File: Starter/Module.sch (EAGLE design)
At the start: 3 parts

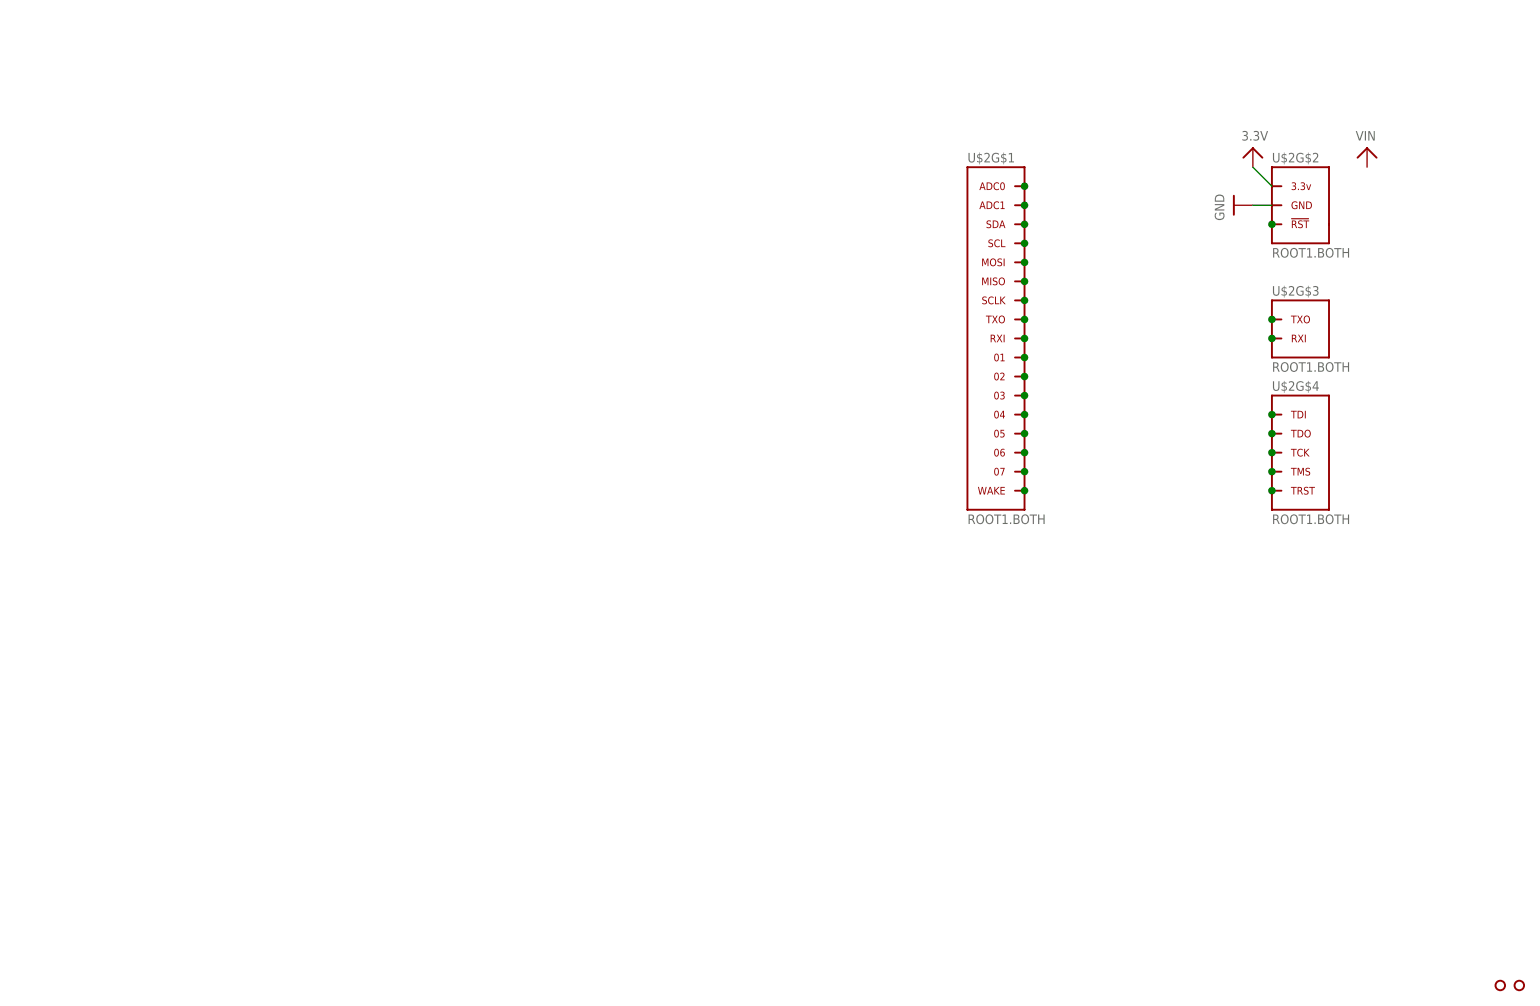
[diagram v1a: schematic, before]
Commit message: Investigating idea to get rid of solder jumpers. Using LoKi Plank scheme of EEPROM and LFSF to auto-assign pins. Also moving to using two connectors instead of one for conector integrety nd module stability. EEPROM: CAT24C02 XOR: NC7S86
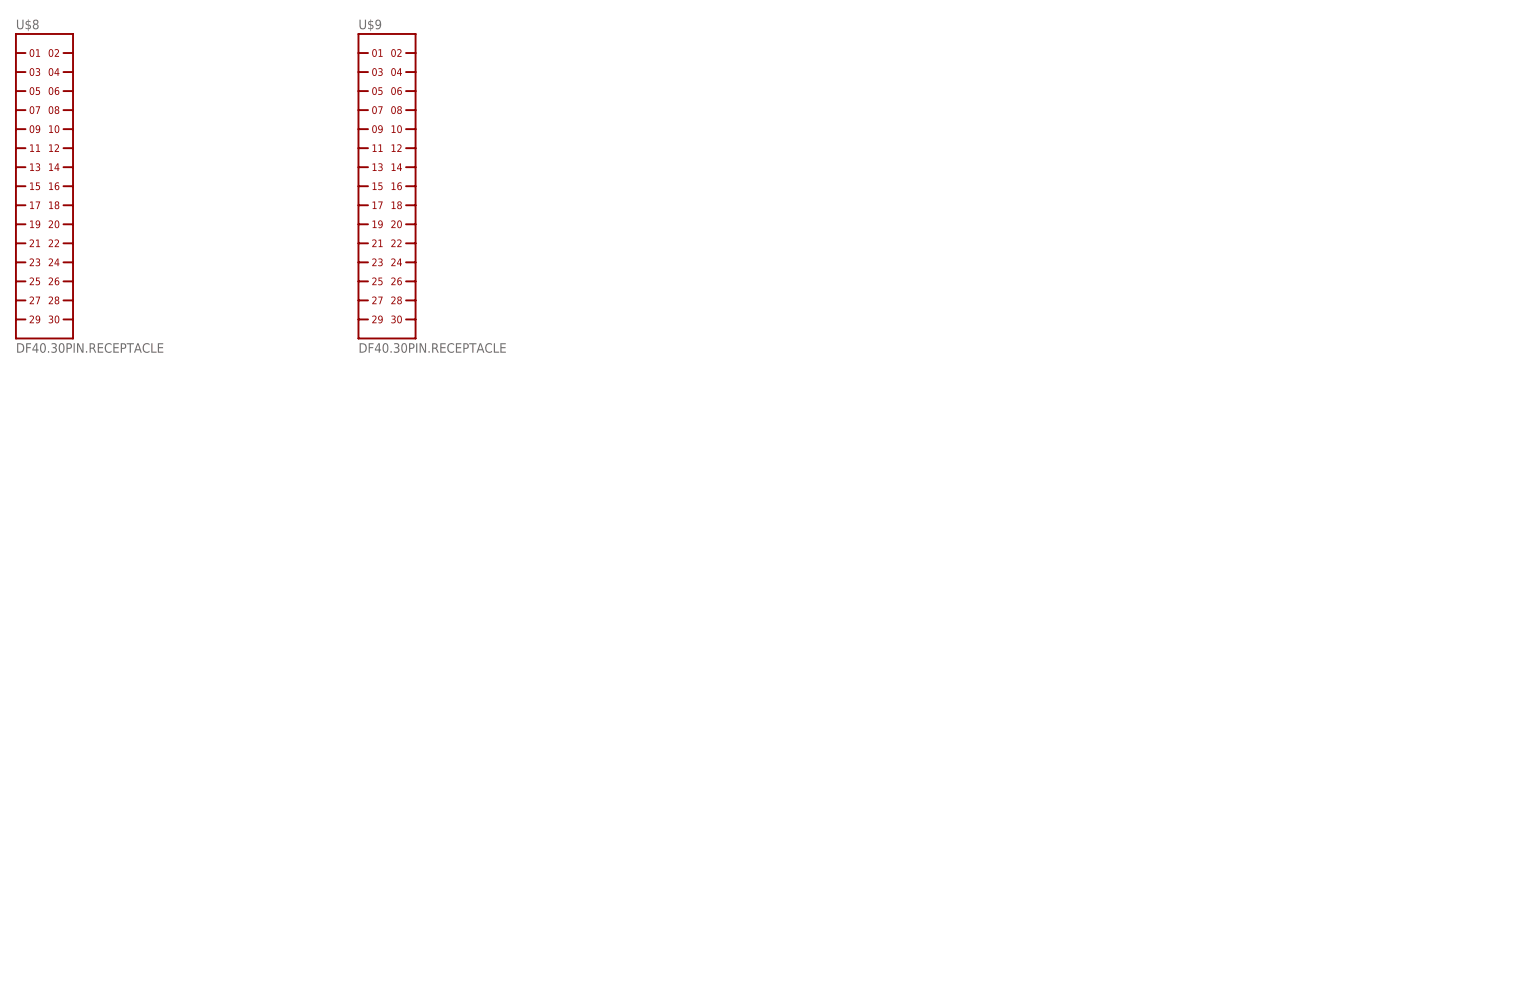
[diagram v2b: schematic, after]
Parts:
- removed U$2: ROOT1.BOTH, thinkmaketest:ROOT1.BOTH
- removed U$3, U$4: HOLE.#2, .screw_holes:HOLE.#2
- added U$8, U$9: DF40.30PIN.RECEPTACLE, hirose:DF40.30PIN.RECEPTACLE
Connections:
- removed net 3.3V: U$2G$2.3.3V
- removed net GND: U$2G$2.GND
- removed net N$1: U$2G$1.04
- removed net N$10: U$2G$1.01
- removed net N$11: U$2G$1.02
- removed net N$12: U$2G$1.MOSI
- removed net N$13: U$2G$1.ADC0
- removed net N$14: U$2G$1.05
- removed net N$15: U$2G$1.06
- removed net N$16: U$2G$1.07
- removed net N$17: U$2G$1.WAKE
- removed net N$18: U$2G$4.TDI
- removed net N$19: U$2G$4.TDO
- removed net N$2: U$2G$1.ADC1
- removed net N$20: U$2G$4.TCK
- removed net N$21: U$2G$4.TMS
- removed net N$22: U$2G$4.TRST
- removed net N$23: U$2G$3.RXI
- removed net N$24: U$2G$3.TXO
- removed net N$25: U$2G$2.!RST
- removed net N$3: U$2G$1.SDA
- removed net N$4: U$2G$1.SCL
- removed net N$5: U$2G$1.03
- removed net N$6: U$2G$1.MISO
- removed net N$7: U$2G$1.SCLK
- removed net N$8: U$2G$1.TXO
- removed net N$9: U$2G$1.RXI
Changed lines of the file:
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@@
 <?xml version="1.0" encoding="utf-8"?>
 <!DOCTYPE eagle SYSTEM "eagle.dtd">
-<eagle version="6.3">
+<eagle version="6.4">
 <drawing>
 <settings>
@@
 <parts>
 <part name="U$1" library="thinkmaketest" deviceset="A4_LAYOUT" device=""/>
-<part name="U$4" library=".screw_holes" deviceset="HOLE" device=".#2" value="HOLE.#2"/>
-<part name="U$5" library="microbuilder" deviceset="GND" device=""/>
-<part name="U$6" library="microbuilder" deviceset="3.3V" device=""/>
-<part name="U$3" library=".screw_holes" deviceset="HOLE" device=".#2" value="HOLE.#2"/>
-<part name="U$2" library="thinkmaketest" deviceset="ROOT1" device=".BOTH"/>
-<part name="U$7" library="microbuilder" deviceset="VIN" device=""/>
+<part name="U$8" library="hirose" deviceset="DF40.30PIN" device=".RECEPTACLE"/>
+<part name="U$9" library="hirose" deviceset="DF40.30PIN" device=".RECEPTACLE"/>
 </parts>
 <sheets>
@@
 <instances>
 <instance part="U$1" gate="G$1" x="0" y="0"/>
-<instance part="U$4" gate="G$1" x="248.92" y="22.86"/>
-<instance part="U$5" gate="G$1" x="213.36" y="127" rot="R270"/>
-<instance part="U$6" gate="G$1" x="215.9" y="132.08"/>
-<instance part="U$3" gate="G$1" x="251.46" y="22.86"/>
-<instance part="U$2" gate="G$1" x="182.88" y="111.76"/>
-<instance part="U$2" gate="G$2" x="218.44" y="127"/>
-<instance part="U$2" gate="G$3" x="220.98" y="109.22"/>
-<instance part="U$2" gate="G$4" x="220.98" y="93.98"/>
-<instance part="U$7" gate="G$1" x="231.14" y="134.62"/>
+<instance part="U$8" gate="U" x="55.88" y="129.54"/>
+<instance part="U$9" gate="U" x="101.6" y="129.54"/>
 </instances>
 <busses>
 </busses>
 <nets>
-<net name="GND" class="0">
-<segment>
-<pinref part="U$5" gate="G$1" pin="GND"/>
-<wire x1="215.9" y1="127" x2="218.44" y2="127" width="0.1524" layer="91"/>
-<pinref part="U$2" gate="G$2" pin="GND"/>
-</segment>
-</net>
-<net name="3.3V" class="0">
-<segment>
-<pinref part="U$6" gate="G$1" pin="3.3V"/>
-<wire x1="218.44" y1="129.54" x2="215.9" y2="132.08" width="0.1524" layer="91"/>
-<pinref part="U$2" gate="G$2" pin="3.3V"/>
-</segment>
-</net>
-<net name="N$2" class="0">
-<segment>
-<pinref part="U$2" gate="G$1" pin="ADC1"/>
-<junction x="185.42" y="127"/>
-</segment>
-</net>
-<net name="N$3" class="0">
-<segment>
-<pinref part="U$2" gate="G$1" pin="SDA"/>
-<junction x="185.42" y="124.46"/>
-</segment>
-</net>
-<net name="N$4" class="0">
-<segment>
-<pinref part="U$2" gate="G$1" pin="SCL"/>
-<junction x="185.42" y="121.92"/>
-</segment>
-</net>
-<net name="N$6" class="0">
-<segment>
-<pinref part="U$2" gate="G$1" pin="MISO"/>
-<junction x="185.42" y="116.84"/>
-</segment>
-</net>
-<net name="N$7" class="0">
-<segment>
-<pinref part="U$2" gate="G$1" pin="SCLK"/>
-<junction x="185.42" y="114.3"/>
-</segment>
-</net>
-<net name="N$9" class="0">
-<segment>
-<pinref part="U$2" gate="G$1" pin="RXI"/>
-<junction x="185.42" y="109.22"/>
-</segment>
-</net>
-<net name="N$10" class="0">
-<segment>
-<pinref part="U$2" gate="G$1" pin="01"/>
-<junction x="185.42" y="106.68"/>
-</segment>
-</net>
-<net name="N$11" class="0">
-<segment>
-<pinref part="U$2" gate="G$1" pin="02"/>
-<junction x="185.42" y="104.14"/>
-</segment>
-</net>
-<net name="N$14" class="0">
-<segment>
-<pinref part="U$2" gate="G$1" pin="05"/>
-<junction x="185.42" y="96.52"/>
-</segment>
-</net>
-<net name="N$15" class="0">
-<segment>
-<pinref part="U$2" gate="G$1" pin="06"/>
-<junction x="185.42" y="93.98"/>
-</segment>
-</net>
-<net name="N$16" class="0">
-<segment>
-<pinref part="U$2" gate="G$1" pin="07"/>
-<junction x="185.42" y="91.44"/>
-</segment>
-</net>
-<net name="N$18" class="0">
-<segment>
-<pinref part="U$2" gate="G$4" pin="TDI"/>
-<junction x="218.44" y="99.06"/>
-</segment>
-</net>
-<net name="N$19" class="0">
-<segment>
-<pinref part="U$2" gate="G$4" pin="TDO"/>
-<junction x="218.44" y="96.52"/>
-</segment>
-</net>
-<net name="N$20" class="0">
-<segment>
-<pinref part="U$2" gate="G$4" pin="TCK"/>
-<junction x="218.44" y="93.98"/>
-</segment>
-</net>
-<net name="N$21" class="0">
-<segment>
-<pinref part="U$2" gate="G$4" pin="TMS"/>
-<junction x="218.44" y="91.44"/>
-</segment>
-</net>
-<net name="N$22" class="0">
-<segment>
-<pinref part="U$2" gate="G$4" pin="TRST"/>
-<junction x="218.44" y="88.9"/>
-</segment>
-</net>
-<net name="N$23" class="0">
-<segment>
-<pinref part="U$2" gate="G$3" pin="RXI"/>
-<junction x="218.44" y="109.22"/>
-</segment>
-</net>
-<net name="N$24" class="0">
-<segment>
-<pinref part="U$2" gate="G$3" pin="TXO"/>
-<junction x="218.44" y="111.76"/>
-</segment>
-</net>
-<net name="N$25" class="0">
-<segment>
-<pinref part="U$2" gate="G$2" pin="!RST"/>
-<junction x="218.44" y="124.46"/>
-</segment>
-</net>
-<net name="N$5" class="0">
-<segment>
-<pinref part="U$2" gate="G$1" pin="03"/>
-<junction x="185.42" y="101.6"/>
-</segment>
-</net>
-<net name="N$8" class="0">
-<segment>
-<pinref part="U$2" gate="G$1" pin="TXO"/>
-<junction x="185.42" y="111.76"/>
-</segment>
-</net>
-<net name="N$1" class="0">
-<segment>
-<pinref part="U$2" gate="G$1" pin="04"/>
-<junction x="185.42" y="99.06"/>
-</segment>
-</net>
-<net name="N$12" class="0">
-<segment>
-<pinref part="U$2" gate="G$1" pin="MOSI"/>
-<junction x="185.42" y="119.38"/>
-</segment>
-</net>
-<net name="N$13" class="0">
-<segment>
-<pinref part="U$2" gate="G$1" pin="ADC0"/>
-<junction x="185.42" y="129.54"/>
-</segment>
-</net>
-<net name="N$17" class="0">
-<segment>
-<pinref part="U$2" gate="G$1" pin="WAKE"/>
-<junction x="185.42" y="88.9"/>
-</segment>
-</net>
 </nets>
 </sheet>
